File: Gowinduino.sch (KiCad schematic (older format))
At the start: 41 parts, among them J1 Power, J2 Analog, J3 Digital, J4 Digital, J5 SPI, J6 JTAG, J8 12V, SW1 Mode, SW2 Reset, U1 GW1NSR-4CQN48P, U2 W25Q32JVSS, U3 TXB0104PW, U4 MP2122, U8 L7805

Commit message: Various touchups around the PCB.
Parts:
- added C22: 10µ, Capacitor_SMD:C_0805_2012Metric_Pad1.18x1.45mm_HandSolder, symbol Device:C_Small
- added C23: 100n, Capacitor_SMD:C_0603_1608Metric_Pad1.08x0.95mm_HandSolder, symbol Device:C_Small
- added L3: 3.3µ, Inductor_SMD:L_0806_2014Metric_Pad1.15x1.60mm_HandSolder, symbol Device:L_Core_Ferrite_Small
- added R13: 36k, Resistor_SMD:R_0603_1608Metric_Pad0.98x0.95mm_HandSolder, symbol Device:R_Small
- added R14: 16k, Resistor_SMD:R_0603_1608Metric_Pad0.98x0.95mm_HandSolder, symbol Device:R_Small
- added R15, R16: 220, Resistor_SMD:R_0603_1608Metric_Pad0.98x0.95mm_HandSolder, symbol Device:R_Small
- added R?: 10k, symbol Device:R_Small
- added U10: SN74AVC4T245PW, Package_SO:TSSOP-16_4.4x5mm_P0.65mm, symbol Logic_LevelTranslator:SN74AVC4T245PW
- added U9: FP6161, Package_TO_SOT_SMD:SOT-23-5, symbol Regulator_Switching:FP6161
- added X1: XO32, Oscillator:Oscillator_SMD_EuroQuartz_XO32-4Pin_3.2x2.5mm, symbol Oscillator:XO32
- L1, L2: value 2.2µH -> 2.2µ; footprint Inductor_SMD:L_0805_2012Metric_Pad1.15x1.40mm_HandSolder -> Inductor_SMD:L_0806_2014Metric_Pad1.15x1.60mm_HandSolder
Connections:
- net +1V8: now also U10.1 (VCCA), U10.3 (2DIR)
- net +3V3: now also C22.1, C23.1, L3.1, R13.1, U10.16 (VCCB), X1.1 (EN), X1.4 (V+)
- net +5V: now also U9.1 (EN), U9.4 (VIN)
- net GND: now also C22.2, C23.2, R14.2, R?.2, U10.14 (2~OE), U10.15 (1~OE), U10.2 (1DIR), U10.7 (2A2), U10.8 (GND), U10.9 (GND), U9.2 (GND), X1.2 (GND)
- net LRX: now also U1.19 (PD13-), U10.5 (1A2); no longer U1.20 (PD16+/GCLK5)
- net LTX: now also U1.18 (PD13+), U10.6 (2A1); no longer U1.21 (PD16-/GCLK5)
- net MCLK: now also U1.20 (PD16+/GCLK5), U10.4 (1A1); no longer U1.22 (PD22+/GCLK4)
- net RX: now also R15.1
- net TCK: now also R?.1
- net TX: now also R16.1
- net ~RST: now also U1.21 (PD16-/GCLK5); no longer U1.23 (PD22-/GCLK4)
- new net: L3.2, U9.3 (LX)
- new net: R13.2, R14.1, U9.5 (FB)
- new net: R16.2, U10.11 (2B1)
- new net: R15.2, U10.12 (1B2)
- new net CLK: U10.13 (1B1), X1.3 (OUT)
- no-connect marks 5 -> 9
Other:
- moved on the sheet: C10, C8, C9, L1, L2, R3, R4, R5, R6, R7, SW2, U4A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

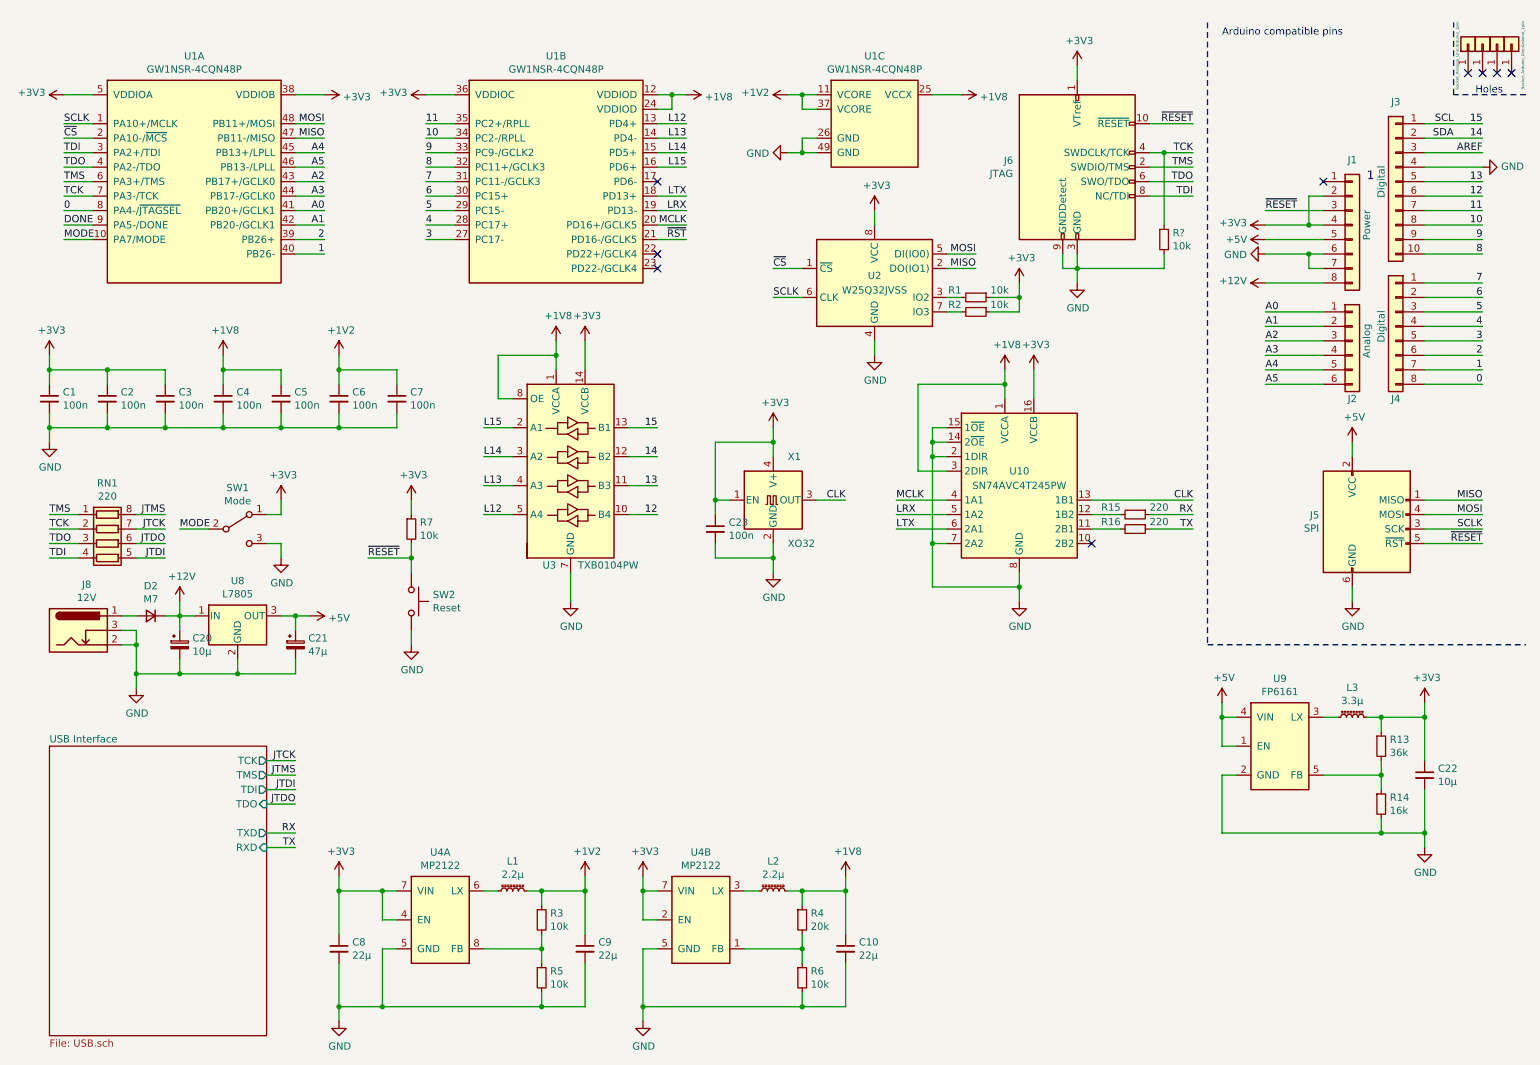
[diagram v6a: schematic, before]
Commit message: Schematics: LEDs
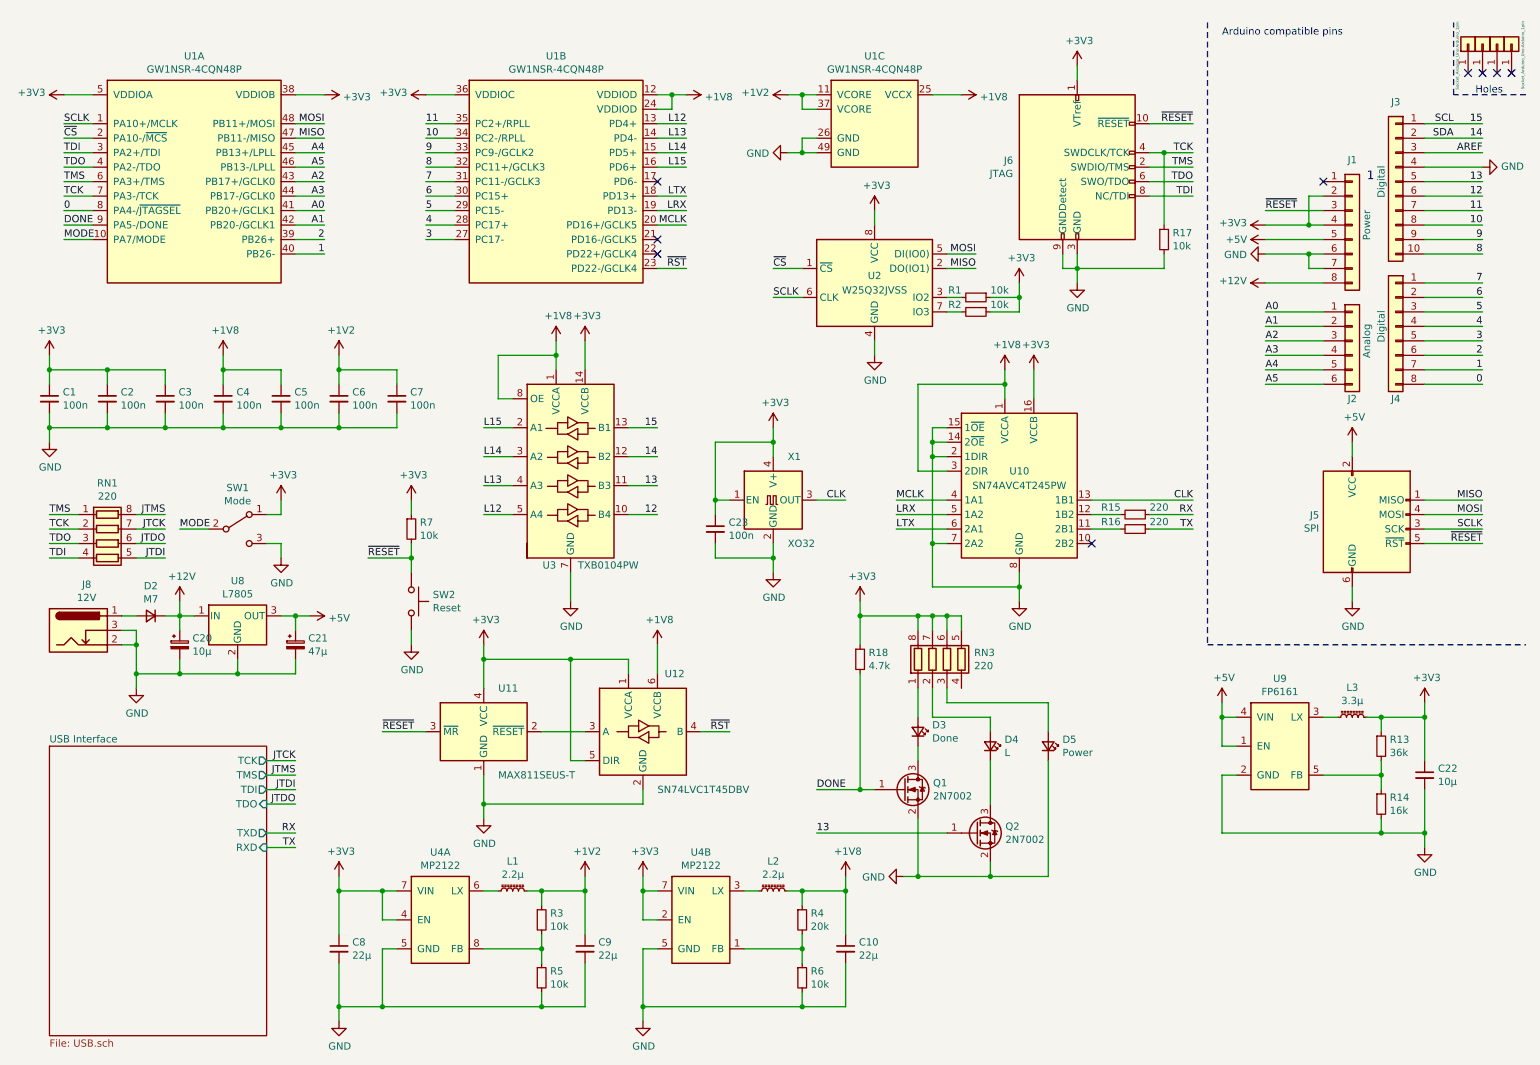
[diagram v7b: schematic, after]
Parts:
- added D3: Done, LED_SMD:LED_0805_2012Metric_Pad1.15x1.40mm_HandSolder, symbol Device:LED_Small
- added D4: L, LED_SMD:LED_0805_2012Metric_Pad1.15x1.40mm_HandSolder, symbol Device:LED_Small
- added D5: Power, LED_SMD:LED_0805_2012Metric_Pad1.15x1.40mm_HandSolder, symbol Device:LED_Small
- added Q1, Q2: 2N7002, Package_TO_SOT_SMD:SOT-23, symbol Transistor_FET:2N7002
- added R18: 4.7k, Resistor_SMD:R_0603_1608Metric_Pad0.98x0.95mm_HandSolder, symbol Device:R_Small
- added RN3: 220, Resistor_SMD:R_Array_Convex_4x0603, symbol Device:R_Pack04
- added U11: MAX811SEUS-T, Package_TO_SOT_SMD:SOT-143, symbol Power_Supervisor:MAX811SEUS-T
- added U12: SN74LVC1T45DBV, Package_TO_SOT_SMD:SOT-23-6, symbol Logic_LevelTranslator:SN74LVC1T45DBV
- R17: renamed from R?; footprint (none) -> Resistor_SMD:R_0603_1608Metric_Pad0.98x0.95mm_HandSolder
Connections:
- net +1V8: now also U12.6 (VCCB)
- net +3V3: now also R18.1, RN3.5 (R4.2), RN3.6 (R3.2), RN3.7 (R2.2), RN3.8 (R1.2), U11.4 (VCC), U12.1 (VCCA), U12.5 (DIR)
- net 13: now also Q2.1 (G)
- net DONE: now also Q1.1 (G), R18.2
- net GND: now also D5.1 (K), Q1.2 (S), Q2.2 (S), U11.1 (GND), U12.2 (GND)
- net ~RESET: now also U11.3 (~MR)
- net ~RST: now also U1.23 (PD22-/GCLK4), U12.4 (B); no longer U1.21 (PD16-/GCLK5)
- new net: U11.2 (~RESET), U12.3 (A)
- new net: D3.1 (K), Q1.3 (D)
- new net: D3.2 (A), RN3.1 (R1.1)
- new net: D4.1 (K), Q2.3 (D)
- new net: D4.2 (A), RN3.2 (R2.1)
- new net: D5.2 (A), RN3.3 (R3.1)

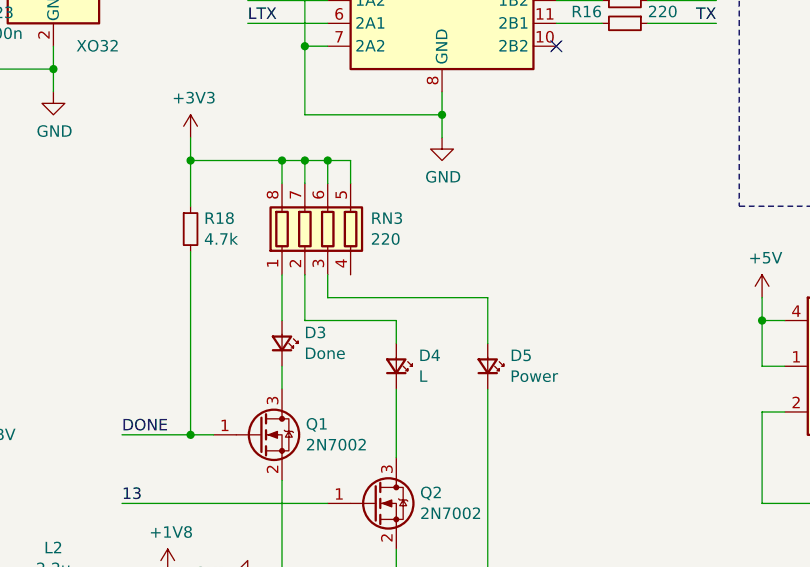
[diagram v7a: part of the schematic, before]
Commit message: PCB: Layout done, now stitching vias
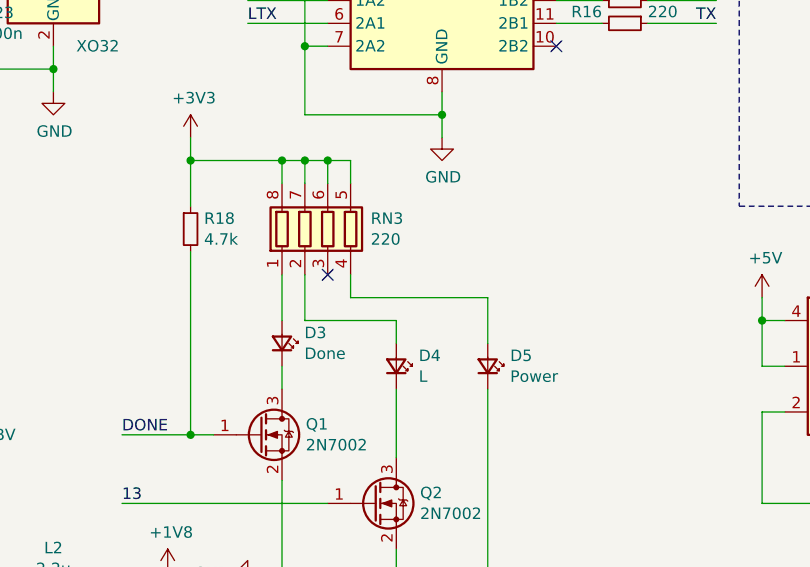
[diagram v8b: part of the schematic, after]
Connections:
- net at D5.2 (A): now also RN3.4 (R4.1); no longer RN3.3 (R3.1)
- no-connect marks 9 -> 10
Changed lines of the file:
@@
 	7500 5300 7500 5400
-Wire Wire Line
-	7200 5100 7200 5200
-Wire Wire Line
-	7200 5200 7900 5200
 Wire Wire Line
 	7900 5200 7900 5400
@@
 Wire Wire Line
 	6300 6100 7200 6100
+Wire Wire Line
+	7300 5100 7300 5200
+Wire Wire Line
+	7300 5200 7900 5200
+NoConn ~ 7200 5100
 $EndSCHEMATC
